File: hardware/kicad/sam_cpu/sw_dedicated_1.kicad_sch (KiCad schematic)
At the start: 74 parts, among them J2 J2 DEDICATED, J3 J3 DEDICATED, U16 74HC165, U17 74HC165

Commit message: Use 3.96 mm KK-396 footprints for the switch harness connectors
J1, J2, J3, J6, J12 and J13 are 0.156" headers on the original board, so
the existing harness plugs need KK-396, as already used for J10 and J11.

Co-Authored-By: Claude Opus 5.5 (1M context) <noreply@anthropic.com>
Claude-Session: https://claude.ai/code/session_019DLTv1F2PjepjxqiUcAMKV
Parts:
- J2: footprint Connector_Molex:Molex_KK-254_AE-6410-12A_1x12_P2.54mm_Vertical -> Connector_Molex:Molex_KK-396_A-41791-0012_1x12_P3.96mm_Vertical
- J3: footprint Connector_Molex:Molex_KK-254_AE-6410-10A_1x10_P2.54mm_Vertical -> Connector_Molex:Molex_KK-396_A-41791-0010_1x10_P3.96mm_Vertical
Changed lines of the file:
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@@
 			)
 		)
-		(property "Footprint" "Connector_Molex:Molex_KK-254_AE-6410-10A_1x10_P2.54mm_Vertical"
+		(property "Footprint" "Connector_Molex:Molex_KK-396_A-41791-0010_1x10_P3.96mm_Vertical"
 			(at 208.28 137.16 0)
 			(hide yes)
@@
 			)
 		)
-		(property "Footprint" "Connector_Molex:Molex_KK-254_AE-6410-12A_1x12_P2.54mm_Vertical"
+		(property "Footprint" "Connector_Molex:Molex_KK-396_A-41791-0012_1x12_P3.96mm_Vertical"
 			(at 15.24 137.16 0)
 			(hide yes)

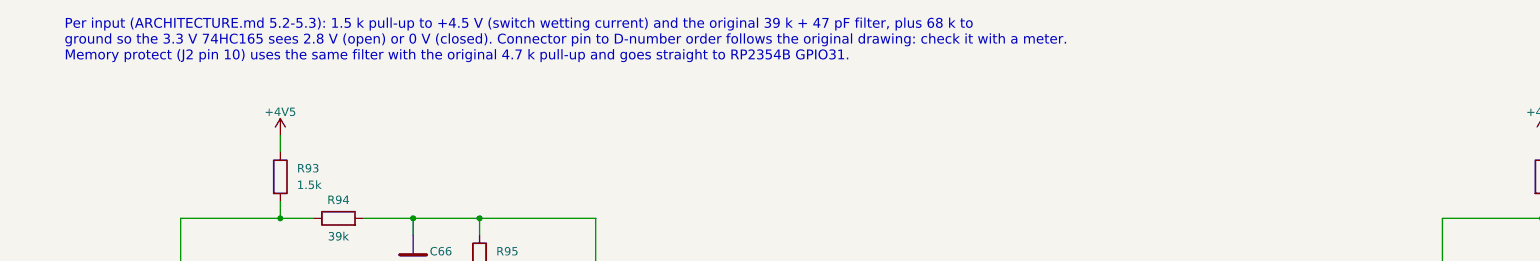
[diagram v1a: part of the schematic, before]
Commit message: Add two HD DMD panels on a PIO parallel bus (incremental edit)
RP2354B GPIO20-36 drive two HUB75 panels (J25/J26) through 3 x 74AHCT245
with shared CLK/LAT/OE and A/B row lines; J5 shares DMD_D0-D6. The 165
load and 595 latch share GPIO17; coin door moves to a 7th 165 (U30),
LED_STATUS and GI_SPARE to a new first 595 (U31). Board widened to 142 mm
below the Pi. Sheets and board edited in place via tools/changes, no
existing footprint moved.

Co-Authored-By: Claude Opus 5.5 (1M context) <noreply@anthropic.com>
Claude-Session: https://claude.ai/code/session_01ExuDVoDDDHhVWjb8EwVzYb
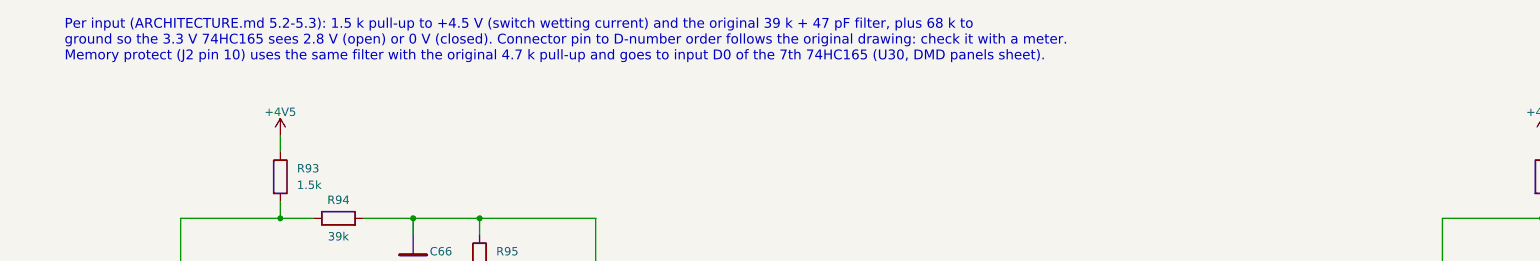
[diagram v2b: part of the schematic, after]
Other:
- note added: "Per input (ARCHITECTURE.md 5.2-5.3): 1.5 k pull-up to +4.5 V (switch wetting current) and the original 39 k + 47 pF filter, plus 68 k to ground so the 3.3 V 74HC165 sees 2.8 V (open) or 0 V (closed). Connector pin to D-number order follows the original drawing: check it with a meter. Memory protect (J2 pin 10) uses the same filter with the original 4.7 k pull-up and goes to input D0 of the 7th 74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"
- note removed: "Per input (ARCHITECTURE.md 5.2-5.3): 1.5 k pull-up to +4.5 V (switch wetting current) and the original 39 k + 47 pF filter, plus 68 k to ground so the 3.3 V 74HC165 sees 2.8 V (open) or 0 V (closed). Connector pin to D-number order follows the original drawing: check it with a meter. Memory protect (J2 pin 10) uses the same filter with the original 4.7 k pull-up and goes straight to RP2354B GPIO3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"
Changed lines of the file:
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@@
 		(company "Stern SAM CPU PPUC (CERN-OHL-S v2)")
 	)
-	(text "Per input (ARCHITECTURE.md 5.2-5.3): 1.5 k pull-up to +4.5 V (switch wetting current) and the original 39 k + 47 pF filter, plus 68 k to\nground so the 3.3 V 74HC165 sees 2.8 V (open) or 0 V (closed). Connector pin to D-number order follows the original drawing: check it with a meter.\nMemory protect (J2 pin 10) uses the same filter with the original 4.7 k pull-up and goes straight to RP2354B GPIO31."
+	(text "Per input (ARCHITECTURE.md 5.2-5.3): 1.5 k pull-up to +4.5 V (switch wetting current) and the original 39 k + 47 pF filter, plus 68 k to\nground so the 3.3 V 74HC165 sees 2.8 V (open) or 0 V (closed). Connector pin to D-number order follows the original drawing: check it with a meter.\nMemory protect (J2 pin 10) uses the same filter with the original 4.7 k pull-up and goes to input D0 of the 7th 74HC165 (U30, DMD panels sheet)."
 		(exclude_from_sim no)
 		(at 15.24 15.24 0)

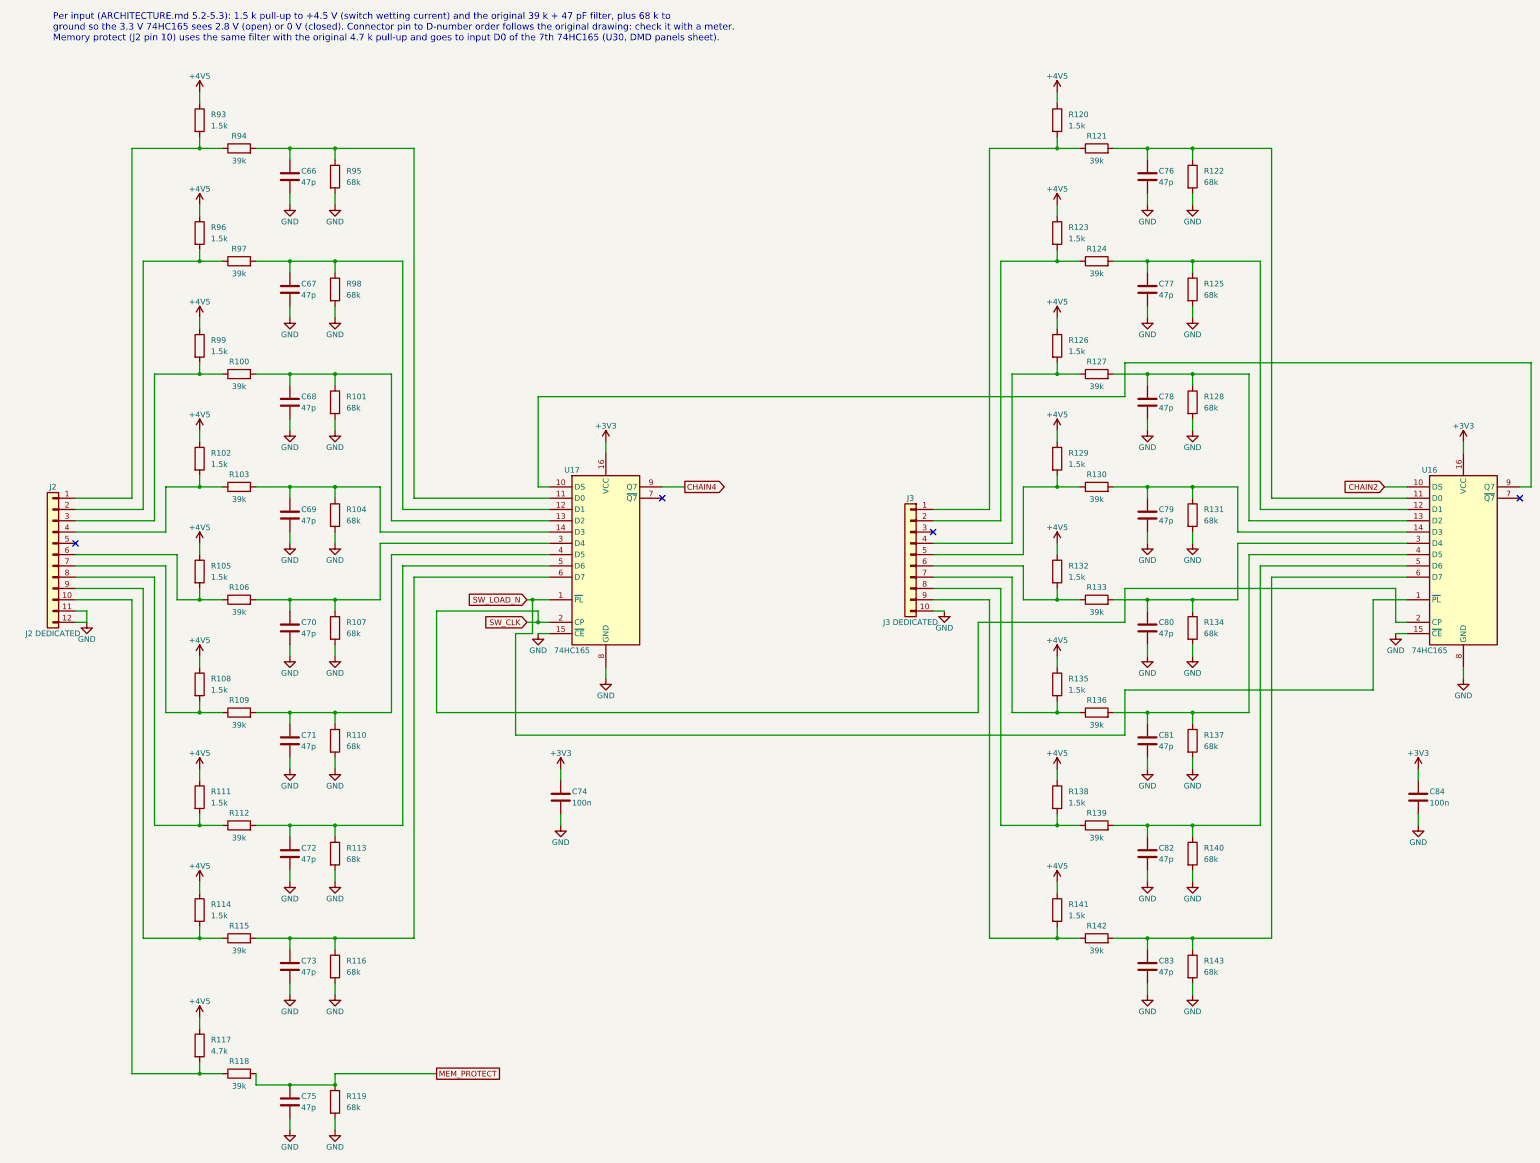
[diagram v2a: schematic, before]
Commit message: DIP switch block not loaded; larger schematic text
c30: SW3, R168-R175, U14 and C93 flagged DNP (schematic and board).
c31: schematic text 1.27 -> 1.6 mm (pins 1.5 mm), intersheet refs moved out.

Co-Authored-By: Claude Opus 5.5 (1M context) <noreply@anthropic.com>
Claude-Session: https://claude.ai/code/session_01ExuDVoDDDHhVWjb8EwVzYb
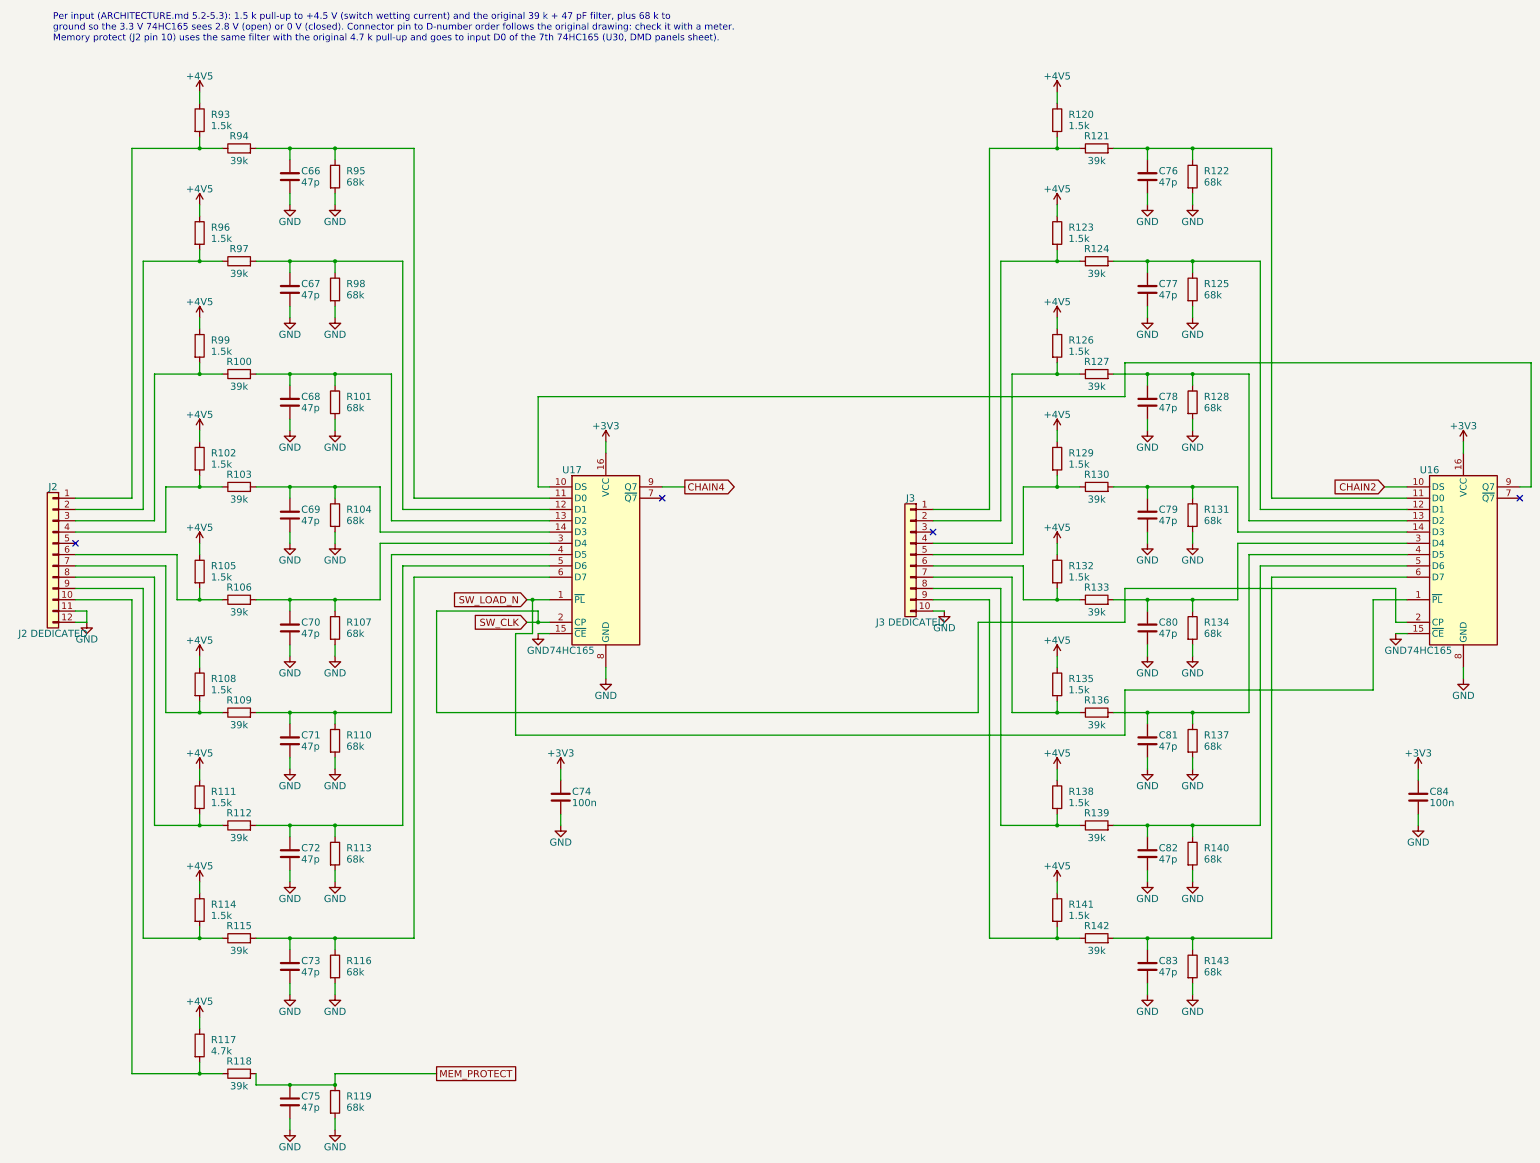
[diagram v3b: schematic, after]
